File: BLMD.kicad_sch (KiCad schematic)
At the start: 8 parts, among them U1 TLP152, U2 TLP152

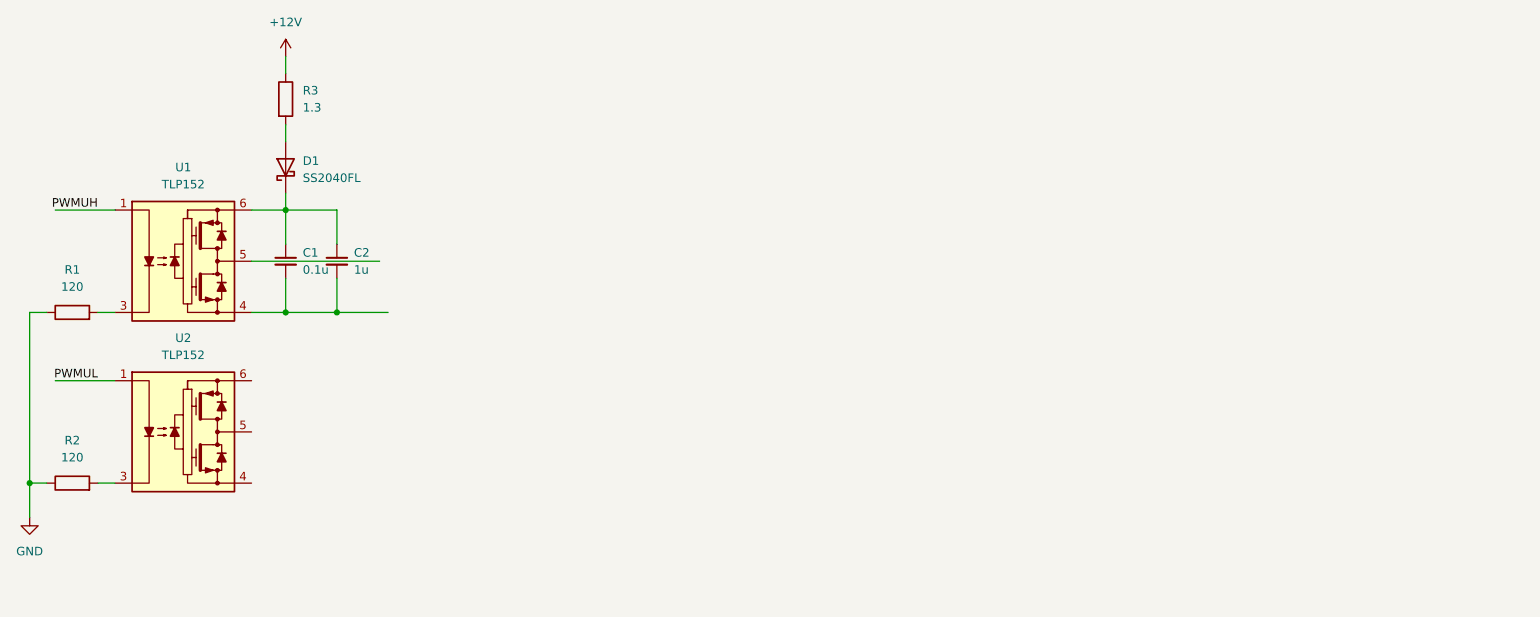
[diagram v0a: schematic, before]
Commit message: chore: Exclude power pin not driven errors in ERC
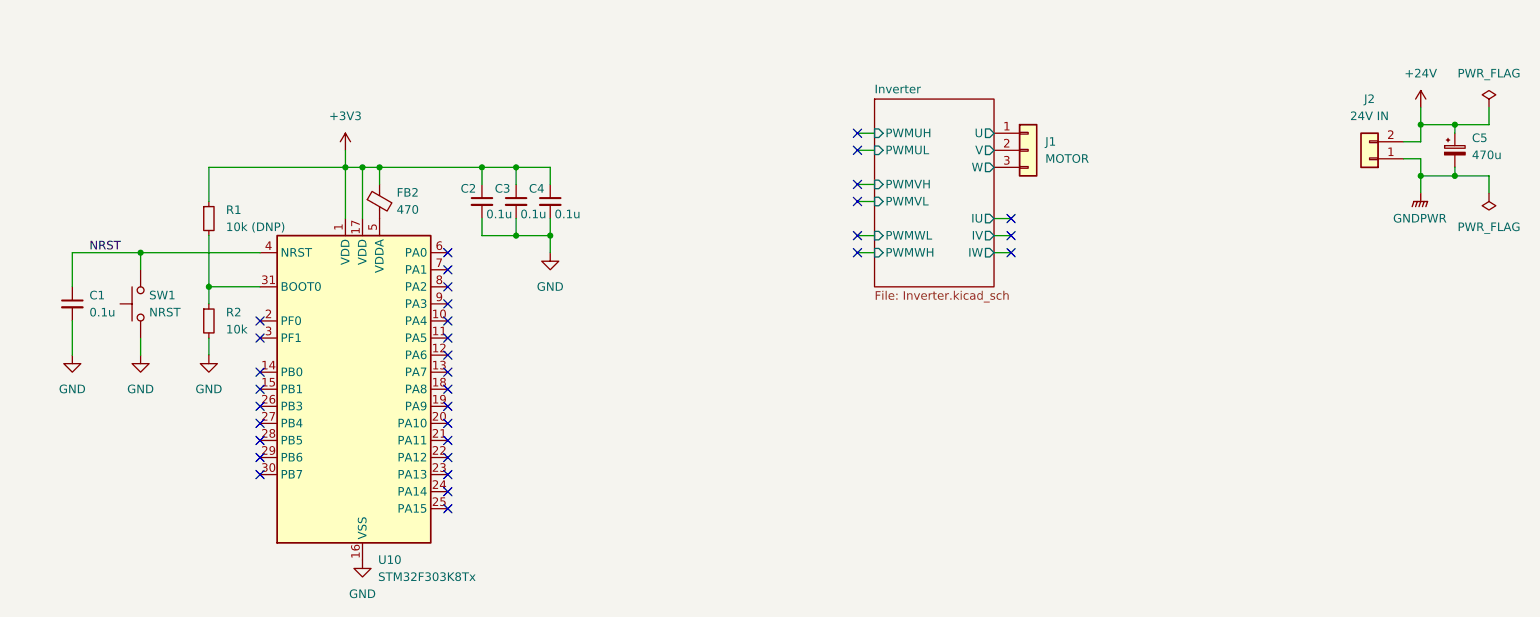
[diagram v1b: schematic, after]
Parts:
- removed D1: SS2040FL, symbol Device:D_Schottky
- removed R1, R2: 120, symbol Device:R
- removed R3: 1.3, symbol Device:R
- removed U1, U2: TLP152, symbol BLMD:TLP152
- added C3, C4: 0.1u, symbol Device:C_Small
- added C5: 470u, symbol Device:C_Polarized_Small
- added FB2: 470, symbol Device:FerriteBead_Small
- added J1: MOTOR, symbol Connector_Generic:Conn_01x03
- added J2: 24V IN, symbol Connector_Generic:Conn_01x02
- added R1: 10k (DNP), symbol Device:R_Small
- added R2: 10k, symbol Device:R_Small
- added SW1: NRST, symbol Switch:SW_Push
- added U10: STM32F303K8Tx, Package_QFP:LQFP-32_7x7mm_P0.8mm, symbol MCU_ST_STM32F3:STM32F303K8Tx
- C2: value 1u -> 0.1u
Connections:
- net GND: now also C1.2, C2.2, C3.2, C4.2, R2.2, SW1.1, U10.16 (VSS), U10.32 (VSS)
- net +3V3: now reaches C2.1
- net +3V3: now also C3.1, C4.1, FB2.1, R1.1, U10.1 (VDD), U10.17 (VDD); no longer C1.1
- new net: FB2.2, U10.5 (VDDA)
- new net: R1.2, R2.1, U10.31 (BOOT0)
- new net +24V: C5.1, J2.2 (Pin_2)
- new net GNDPWR: C5.2, J2.1 (Pin_1)
- new net Inverter/U: J1.1 (Pin_1)
- new net Inverter/V: J1.2 (Pin_2)
- new net Inverter/W: J1.3 (Pin_3)
- new net NRST: C1.1, SW1.2, U10.4 (NRST)
- no-connect marks 0 -> 34
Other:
- added sheet Inverter (Inverter.kicad_sch)

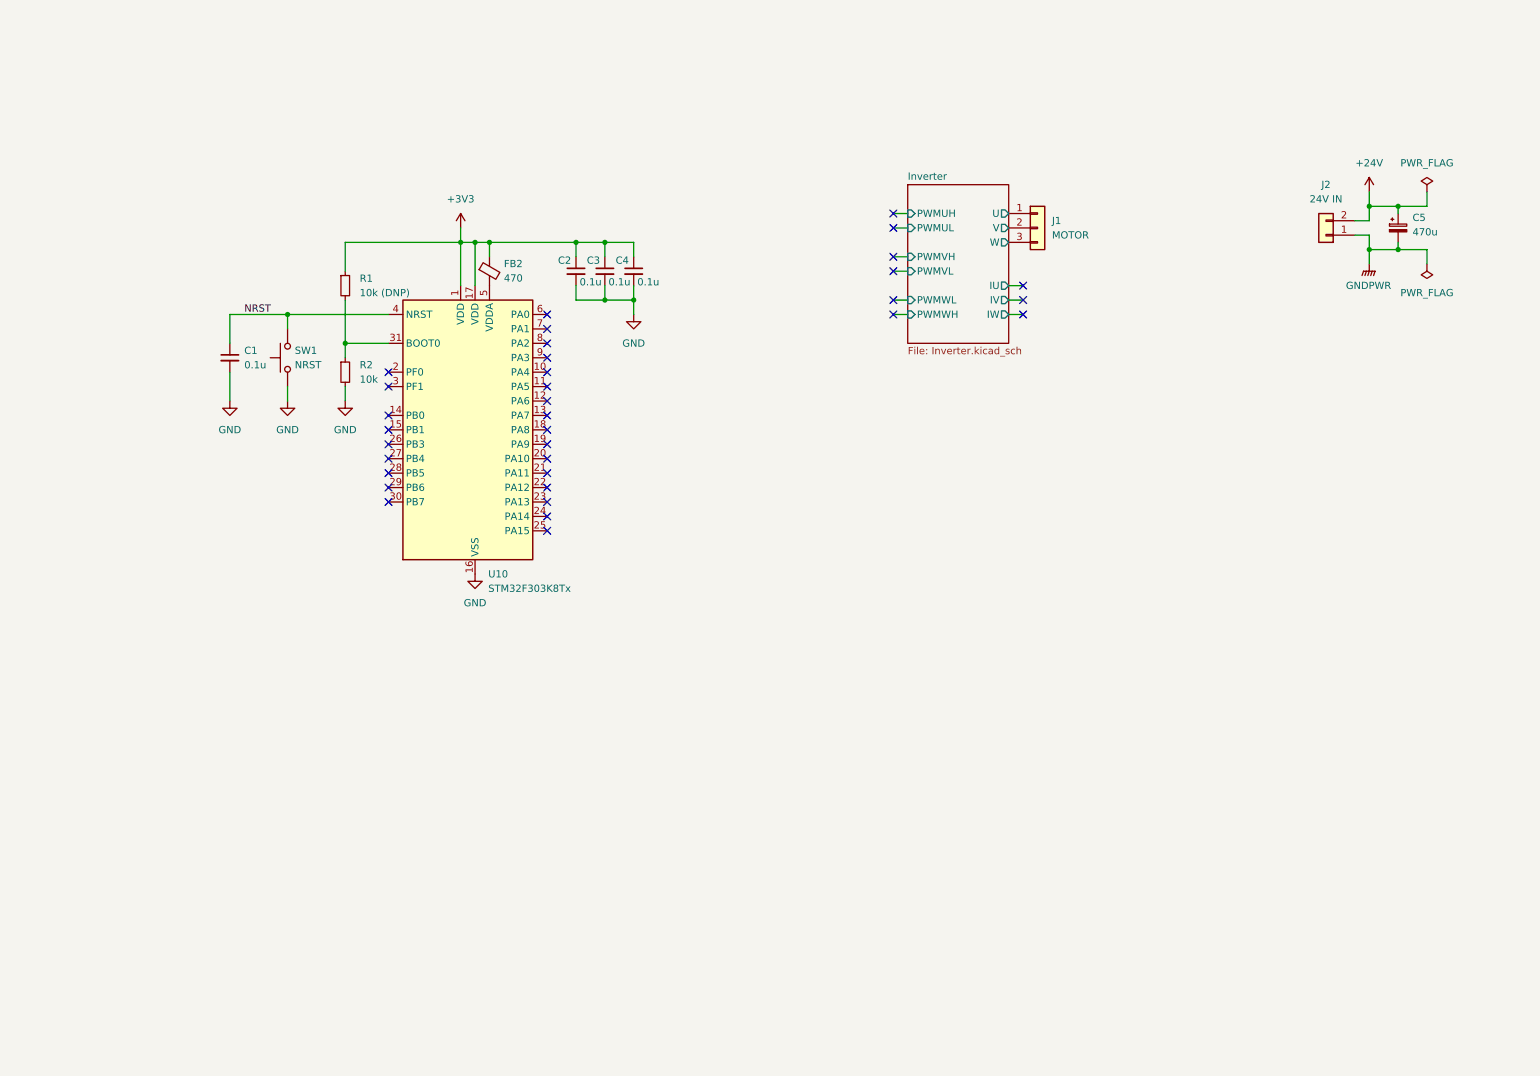
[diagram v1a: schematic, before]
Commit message: feat: Add symbols for BD41044FJ-C and NJM12877
The commit adds symbols for the BD41044FJ-C and NJM12877 components to the KiCad project.
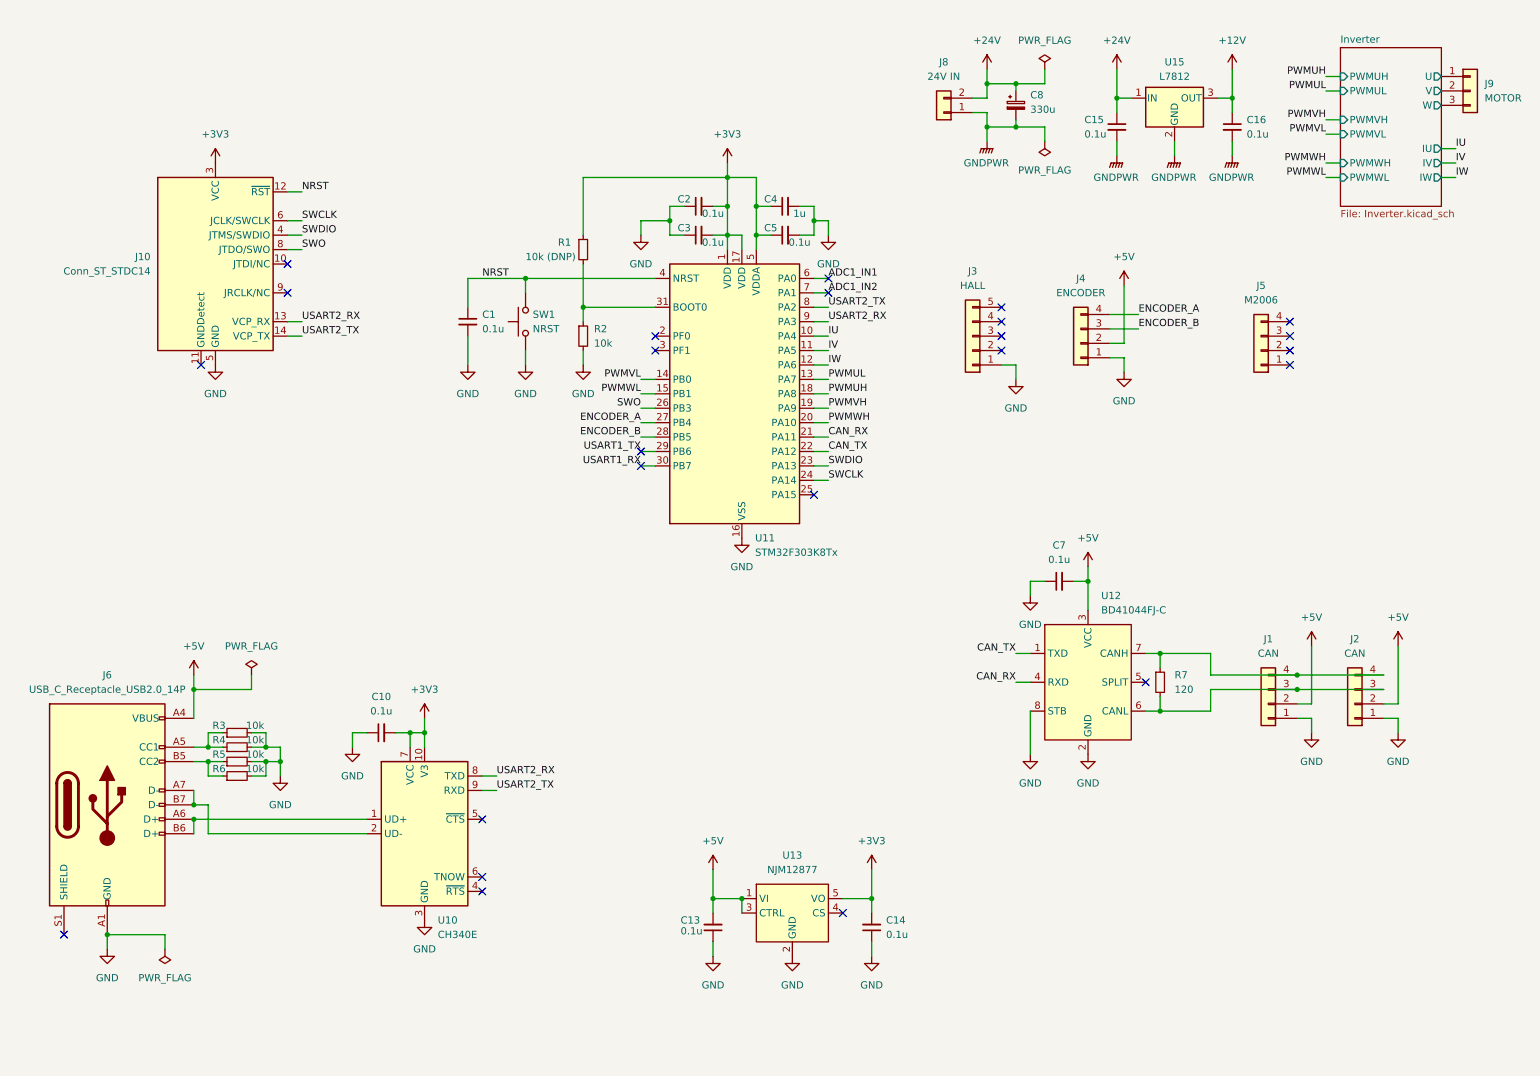
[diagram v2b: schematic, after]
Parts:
- removed FB2: 470, symbol Device:FerriteBead_Small
- added C10, C13, C14, C15, C16, C5, C7: 0.1u, Capacitor_SMD:C_0603_1608Metric_Pad1.08x0.95mm_HandSolder, symbol Device:C_Small
- added J1, J2: CAN, symbol Connector_Generic:Conn_01x04
- added J10: Conn_ST_STDC14, symbol Connector:Conn_ST_STDC14
- added J3: HALL, symbol Connector_Generic:Conn_01x05
- added J4: ENCODER, symbol Connector_Generic:Conn_01x04
- added J5: M2006, symbol Connector_Generic:Conn_01x04
- added J6: USB_C_Receptacle_USB2.0_14P, Connector_USB:USB_C_Receptacle_GCT_USB4105-xx-A_16P_TopMnt_Horizontal, symbol Connector:USB_C_Receptacle_USB2.0_14P
- added R3, R4, R5, R6: 10k, Resistor_SMD:R_0603_1608Metric_Pad0.98x0.95mm_HandSolder, symbol Device:R_Small
- added R7: 120, Resistor_SMD:R_0603_1608Metric_Pad0.98x0.95mm_HandSolder, symbol Device:R_Small
- added U10: CH340E, Package_SO:MSOP-10_3x3mm_P0.5mm, symbol Interface_USB:CH340E
- added U12: BD41044FJ-C, Package_SO:SOP-8_3.9x4.9mm_P1.27mm, symbol BLMD:BD41044FJ-C
- added U13: NJM12877, Package_TO_SOT_SMD:SOT-23-5_HandSoldering, symbol BLMD:NJM12877
- added U15: L7812, Package_TO_SOT_THT:TO-220-3_Vertical, symbol Regulator_Linear:L7812
- C1, C2, C3: footprint (none) -> Capacitor_SMD:C_0603_1608Metric_Pad1.08x0.95mm_HandSolder
- C4: value 0.1u -> 1u; footprint (none) -> Capacitor_SMD:C_0603_1608Metric_Pad1.08x0.95mm_HandSolder
- C8: renamed from C5; value 470u -> 330u; footprint (none) -> Capacitor_SMD:CP_Elec_10x10.5
- J8: renamed from J2; footprint (none) -> Connector_AMASS:AMASS_XT60PW-M_1x02_P7.20mm_Horizontal
- J9: renamed from J1; footprint (none) -> Connector_Wire:SolderWire-1sqmm_1x03_P5.4mm_D1.4mm_OD2.7mm
- R1, R2: footprint (none) -> Resistor_SMD:R_0603_1608Metric_Pad0.98x0.95mm_HandSolder
- SW1: footprint (none) -> Button_Switch_THT:SW_PUSH_1P1T_6x3.5mm_H4.3_APEM_MJTP1243
- renumbered U10 to U11
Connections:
- net +24V: now also C15.1, U15.1 (IN)
- net +3V3: now also C2.2, C3.2, U11.5 (VDDA), C10.2, C14.2, C5.1, J10.3 (VCC), U10.10 (V3), U10.7 (VCC), U13.5 (VO); no longer C2.1, C3.1
- net GND: now also C2.1, C3.1, C10.1, C13.1, C14.1, C5.2, C7.1, J1.1 (Pin_1), J10.5 (GND), J10.7 (GND), J2.1 (Pin_1), J3.1 (Pin_1), J4.1 (Pin_1), J6.A1 (GND), J6.A12 (GND), J6.B1 (GND), J6.B12 (GND), R3.2, R4.2, R5.2, R6.2, U10.3 (GND), U12.2 (GND), U12.8 (STB), U13.2 (GND); no longer C2.2, C3.2
- net GNDPWR: now also C15.2, C16.2, U15.2 (GND)
- net NRST: now also J10.12 (~{RST})
- net IU: now reaches U11.10 (PA4)
- net IV: now reaches U11.11 (PA5)
- net IW: now reaches U11.12 (PA6)
- net PWMUL: now reaches U11.13 (PA7)
- net PWMVL: now reaches U11.14 (PB0)
- net PWMWL: now reaches U11.15 (PB1)
- net PWMUH: now reaches U11.18 (PA8)
- net PWMVH: now reaches U11.19 (PA9)
- net PWMWH: now reaches U11.20 (PA10)
- net CAN_RX: now reaches U11.21 (PA11)
- net CAN_RX: now also U12.4 (RXD)
- net CAN_TX: now reaches U11.22 (PA12)
- net CAN_TX: now also U12.1 (TXD)
- net SWDIO: now reaches U11.23 (PA13)
- net SWDIO: now also J10.4 (JTMS/SWDIO)
- net SWCLK: now reaches U11.24 (PA14)
- net SWCLK: now also J10.6 (JCLK/SWCLK)
- net SWO: now reaches U11.26 (PB3)
- net SWO: now also J10.8 (JTDO/SWO)
- net ENCODER_A: now reaches U11.27 (PB4)
- net ENCODER_A: now also J4.4 (Pin_4)
- net ENCODER_B: now reaches U11.28 (PB5)
- net ENCODER_B: now also J4.3 (Pin_3)
- net USART1_TX: now reaches U11.29 (PB6)
- net USART1_RX: now reaches U11.30 (PB7)
- net ADC1_IN1: now reaches U11.6 (PA0)
- net ADC1_IN2: now reaches U11.7 (PA1)
- net USART2_TX: now reaches U11.8 (PA2)
- net USART2_TX: now also J10.14 (VCP_TX), U10.9 (RXD)
- net USART2_RX: now reaches U11.9 (PA3)
- net USART2_RX: now also J10.13 (VCP_RX), U10.8 (TXD)
- new net: J6.B5 (CC2), R5.1, R6.1
- new net: J1.3 (Pin_3), J2.3 (Pin_3), R7.2, U12.6 (CANL)
- new net: J1.4 (Pin_4), J2.4 (Pin_4), R7.1, U12.7 (CANH)
- new net: J6.A6 (D+), J6.B6 (D+), U10.1 (UD+)
- new net: J6.A7 (D-), J6.B7 (D-), U10.2 (UD-)
- new net: J6.A5 (CC1), R3.1, R4.1
- new net +12V: C16.1, U15.3 (OUT)
- new net +5V: C13.2, C7.2, J1.2 (Pin_2), J2.2 (Pin_2), J4.2 (Pin_2), J6.A4 (VBUS), J6.A9 (VBUS), J6.B4 (VBUS), J6.B9 (VBUS), U12.3 (VCC), U13.1 (VI), U13.3 (CTRL)
- no-connect marks 34 -> 24
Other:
- moved on the sheet: C1, C8, J8, J9, R1, R2, SW1, U11
